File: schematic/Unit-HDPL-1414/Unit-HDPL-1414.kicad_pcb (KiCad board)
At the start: 2 copper layers, 76.5 x 20.6 mm, 5 parts, among them J1 Conn_01x04, U1 M5StampS3, U2 HPDL-1414, U3 HPDL-1414

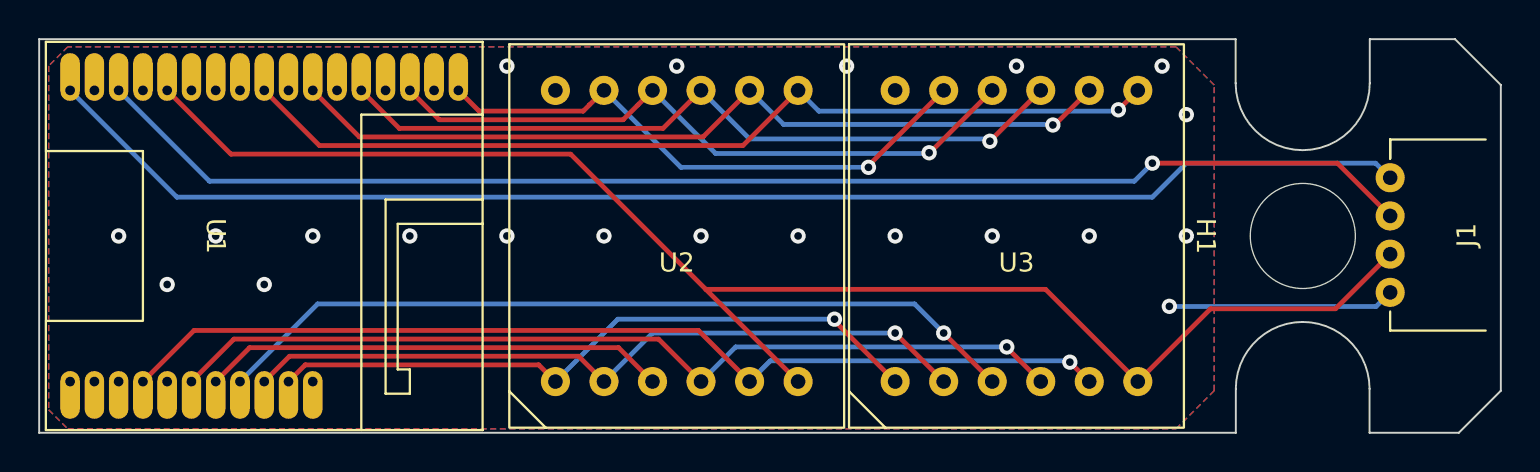
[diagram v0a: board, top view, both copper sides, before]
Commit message: 基板ピン配置ミス修正
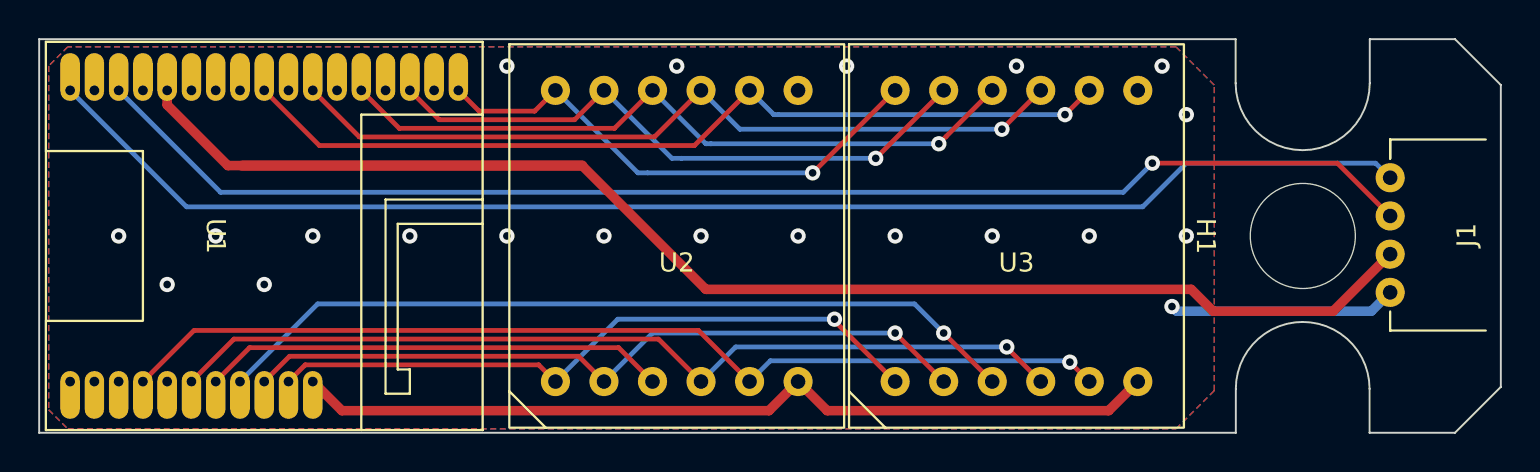
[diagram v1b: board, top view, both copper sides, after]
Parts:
- U2, U3: value HPDL-1414 -> hpdl1414
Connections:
- U1 pad 28: unconnected-(U1-3V3-Pad28) -> +3.3V
- U2 pad 11: Net-(U1-G7) -> Net-(U1-G3)
- U2 pad 12: Net-(U1-G9) -> Net-(U1-G1)
- U2 pad 6: +5V -> +3.3V
- U2 pad 8: Net-(U1-G1) -> Net-(U1-G9)
- U2 pad 9: Net-(U1-G3) -> Net-(U1-G7)
- U3 pad 11: Net-(U1-G7) -> Net-(U1-G3)
- U3 pad 12: Net-(U1-G9) -> Net-(U1-G1)
- U3 pad 6: +5V -> +3.3V
- U3 pad 8: Net-(U1-G1) -> Net-(U1-G9)
- U3 pad 9: Net-(U1-G3) -> Net-(U1-G7)
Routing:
- net +3.3V: track 0.00 -> 45.7 mm
- net +5V: track 81.4 -> 71.9 mm
- net Net-(U1-G5): track 39.4 -> 37.0 mm
- net Net-(U1-G9): track 49.0 -> 46.6 mm
- net Net-(U1-G7): track 44.2 -> 41.8 mm
- net Net-(U1-G1): track 29.7 -> 27.3 mm
- net Net-(U1-G3): track 34.5 -> 32.2 mm
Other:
- outline, holes or cut-outs redrawn
- board text added: "Unit HPDL1414 Ver.0.1"
